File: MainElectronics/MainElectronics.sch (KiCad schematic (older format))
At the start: 11 parts

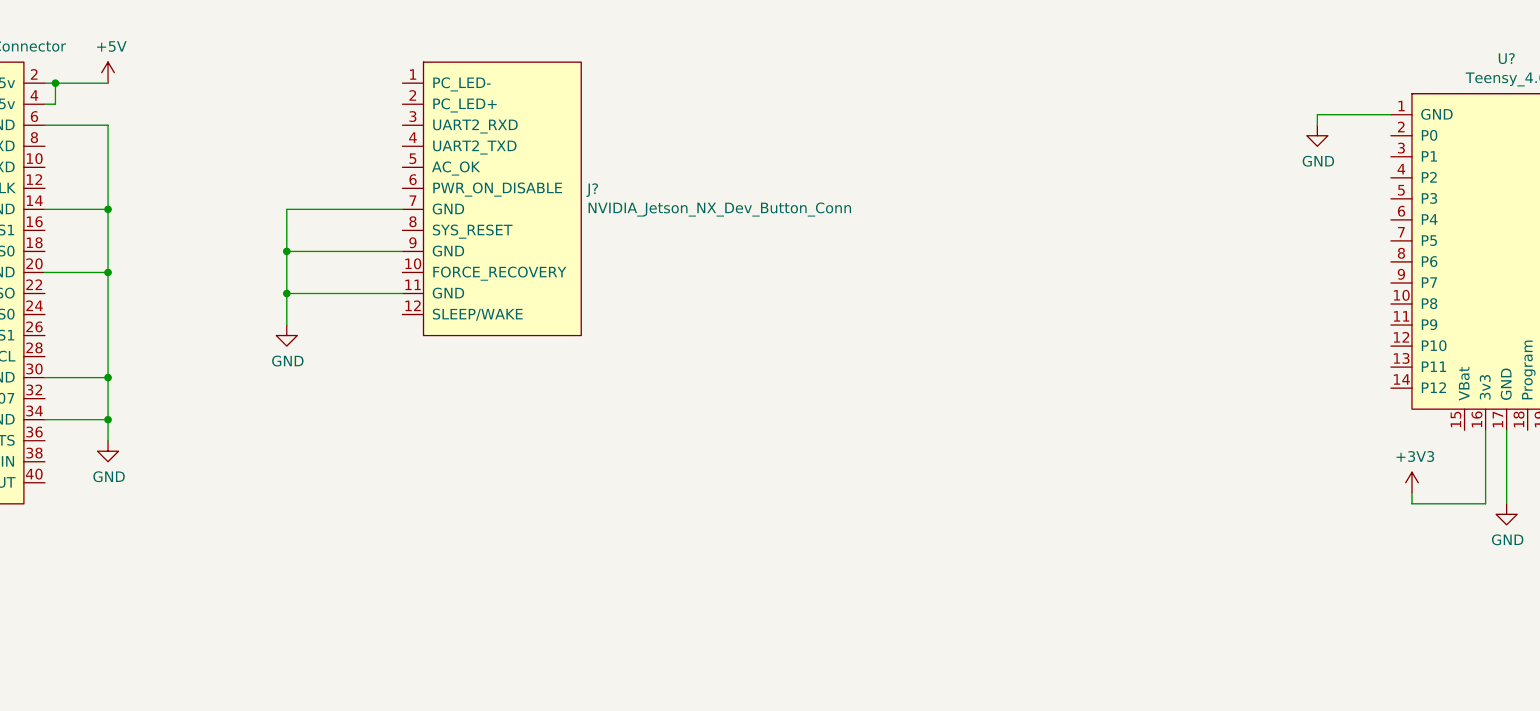
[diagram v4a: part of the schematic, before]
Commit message: Connected Jetson and Teensy
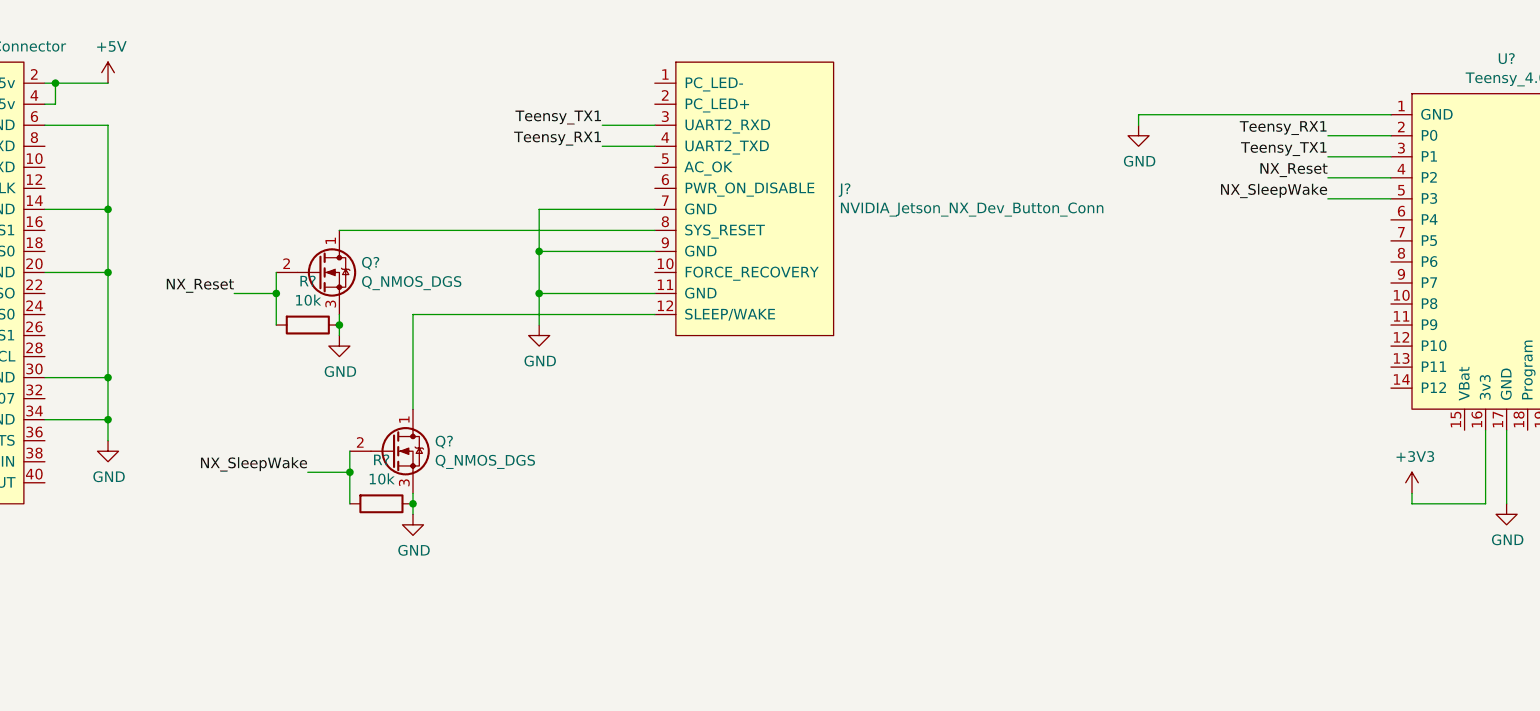
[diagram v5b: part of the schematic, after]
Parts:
- added Q? (x2): Q_NMOS_DGS, symbol Device:Q_NMOS_DGS
- added R? (x2): 10k, symbol Device:R
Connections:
- net GND: now also Q?.3 (S), Q?.3 (S), R?.1, R?.1
- net at J?.12 (SLEEP/WAKE): now also Q?.1 (D)
- net Teensy_TX1: now reaches J?.3 (UART2_RXD)
- net Teensy_TX1: now also U?.3 (P1)
- net Teensy_RX1: now reaches J?.4 (UART2_TXD)
- net Teensy_RX1: now also U?.2 (P0)
- net at J?.8 (SYS_RESET): now also Q?.1 (D)
- net NX_Reset: now reaches U?.4 (P2)
- net NX_Reset: now also Q?.2 (G), R?.2
- net NX_SleepWake: now reaches U?.5 (P3)
- net NX_SleepWake: now also Q?.2 (G), R?.2
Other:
- moved on the sheet: J?
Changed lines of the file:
@@
 L MainElectronicsLib:NVIDIA_Jetson_NX_Dev_Button_Conn J?
 U 1 1 5ED74642
-P 5500 2750
-F 0 "J?" H 5928 3046 50  0000 L CNN
-F 1 "NVIDIA_Jetson_NX_Dev_Button_Conn" H 5928 2955 50  0000 L CNN
-F 2 "" H 5500 3700 50  0001 C CNN
-F 3 "" H 5500 3700 50  0001 C CNN
-	1    5500 2750
+P 6700 2750
+F 0 "J?" H 7128 3046 50  0000 L CNN
+F 1 "NVIDIA_Jetson_NX_Dev_Button_Conn" H 7128 2955 50  0000 L CNN
+F 2 "" H 6700 3700 50  0001 C CNN
+F 3 "" H 6700 3700 50  0001 C CNN
+	1    6700 2750
 	1    0    0    -1
 $EndComp
@@
 L power:GND #PWR?
 U 1 1 5EDF91C0
-P 4500 3100
-F 0 "#PWR?" H 4500 2850 50  0001 C CNN
-F 1 "GND" H 4505 2927 50  0000 C CNN
-F 2 "" H 4500 3100 50  0001 C CNN
-F 3 "" H 4500 3100 50  0001 C CNN
-	1    4500 3100
-	1    0    0    -1
-$EndComp
-Wire Wire Line
-	5050 2550 4500 2550
-Wire Wire Line
-	4500 2550 4500 2750
-Wire Wire Line
-	5050 2750 4500 2750
-Connection ~ 4500 2750
-Wire Wire Line
-	4500 2750 4500 2950
-Wire Wire Line
-	5050 2950 4500 2950
-Connection ~ 4500 2950
-Wire Wire Line
-	4500 2950 4500 3100
+P 5700 3100
+F 0 "#PWR?" H 5700 2850 50  0001 C CNN
+F 1 "GND" H 5705 2927 50  0000 C CNN
+F 2 "" H 5700 3100 50  0001 C CNN
+F 3 "" H 5700 3100 50  0001 C CNN
+	1    5700 3100
+	1    0    0    -1
+$EndComp
+Wire Wire Line
+	6250 2550 5700 2550
+Wire Wire Line
+	5700 2550 5700 2750
+Wire Wire Line
+	6250 2750 5700 2750
+Connection ~ 5700 2750
+Wire Wire Line
+	5700 2750 5700 2950
+Wire Wire Line
+	6250 2950 5700 2950
+Connection ~ 5700 2950
+Wire Wire Line
+	5700 2950 5700 3100
 $Comp
 L power:GND #PWR?
 U 1 1 5EDFB035
-P 9400 2150
-F 0 "#PWR?" H 9400 1900 50  0001 C CNN
-F 1 "GND" H 9405 1977 50  0000 C CNN
-F 2 "" H 9400 2150 50  0001 C CNN
-F 3 "" H 9400 2150 50  0001 C CNN
-	1    9400 2150
-	1    0    0    -1
-$EndComp
-Wire Wire Line
-	9750 2100 9400 2100
-Wire Wire Line
-	9400 2100 9400 2150
+P 8550 2150
+F 0 "#PWR?" H 8550 1900 50  0001 C CNN
+F 1 "GND" H 8555 1977 50  0000 C CNN
+F 2 "" H 8550 2150 50  0001 C CNN
+F 3 "" H 8550 2150 50  0001 C CNN
+	1    8550 2150
+	1    0    0    -1
+$EndComp
+Wire Wire Line
+	9750 2100 8550 2100
+Wire Wire Line
+	8550 2100 8550 2150
 $Comp
 L power:GND #PWR?
@@
 Text Label 11050 3000 0    50   ~ 0
 NEOPIXEL_DIN
+Wire Wire Line
+	9750 2200 9450 2200
+Wire Wire Line
+	9750 2300 9450 2300
+Text Label 9450 2200 2    50   ~ 0
+Teensy_RX1
+Text Label 9450 2300 2    50   ~ 0
+Teensy_TX1
+Text Label 6000 2250 2    50   ~ 0
+Teensy_RX1
+Text Label 6000 2150 2    50   ~ 0
+Teensy_TX1
+Wire Wire Line
+	6000 2150 6250 2150
+Wire Wire Line
+	6250 2250 6000 2250
+Wire Wire Line
+	6250 2650 4750 2650
+Wire Wire Line
+	5100 3500 5100 3050
+Wire Wire Line
+	5100 3050 6250 3050
+$Comp
+L power:GND #PWR?
+U 1 1 5EE9D355
+P 5100 4000
+F 0 "#PWR?" H 5100 3750 50  0001 C CNN
+F 1 "GND" H 5105 3827 50  0000 C CNN
+F 2 "" H 5100 4000 50  0001 C CNN
+F 3 "" H 5100 4000 50  0001 C CNN
+	1    5100 4000
+	1    0    0    -1
+$EndComp
+Wire Wire Line
+	5100 4000 5100 3950
+$Comp
+L Device:R R?
+U 1 1 5EEA2232
+P 4950 3950
+F 0 "R?" V 4743 3950 50  0000 C CNN
+F 1 "10k" V 4834 3950 50  0000 C CNN
+F 2 "" V 4880 3950 50  0001 C CNN
+F 3 "~" H 4950 3950 50  0001 C CNN
+	1    4950 3950
+	0    1    1    0
+$EndComp
+Connection ~ 5100 3950
+Wire Wire Line
+	5100 3950 5100 3900
+Wire Wire Line
+	4800 3950 4800 3800
+Wire Wire Line
+	4800 3800 4600 3800
+Connection ~ 4800 3800
+Wire Wire Line
+	4800 3800 4800 3700
+Text Label 4600 3800 2    50   ~ 0
+NX_SleepWake
+Text Label 4250 2950 2    50   ~ 0
+NX_Reset
+Wire Wire Line
+	4450 2950 4450 3100
+Connection ~ 4450 2950
+Wire Wire Line
+	4450 2950 4250 2950
+Wire Wire Line
+	4450 2850 4450 2950
+Wire Wire Line
+	4750 3100 4750 3050
+Connection ~ 4750 3100
+$Comp
+L Device:R R?
+U 1 1 5EEA357F
+P 4600 3100
+F 0 "R?" V 4393 3100 50  0000 C CNN
+F 1 "10k" V 4484 3100 50  0000 C CNN
+F 2 "" V 4530 3100 50  0001 C CNN
+F 3 "~" H 4600 3100 50  0001 C CNN
+	1    4600 3100
+	0    1    1    0
+$EndComp
+Wire Wire Line
+	4750 3150 4750 3100
+$Comp
+L power:GND #PWR?
+U 1 1 5EE9D73F
+P 4750 3150
+F 0 "#PWR?" H 4750 2900 50  0001 C CNN
+F 1 "GND" H 4755 2977 50  0000 C CNN
+F 2 "" H 4750 3150 50  0001 C CNN
+F 3 "" H 4750 3150 50  0001 C CNN
+	1    4750 3150
+	1    0    0    -1
+$EndComp
+$Comp
+L Device:Q_NMOS_DGS Q?
+U 1 1 5EE9639C
+P 5000 3700
+F 0 "Q?" H 5204 3746 50  0000 L CNN
+F 1 "Q_NMOS_DGS" H 5204 3655 50  0000 L CNN
+F 2 "" H 5200 3800 50  0001 C CNN
+F 3 "~" H 5000 3700 50  0001 C CNN
+	1    5000 3700
+	1    0    0    -1
+$EndComp
+$Comp
+L Device:Q_NMOS_DGS Q?
+U 1 1 5EE91588
+P 4650 2850
+F 0 "Q?" H 4854 2896 50  0000 L CNN
+F 1 "Q_NMOS_DGS" H 4854 2805 50  0000 L CNN
+F 2 "" H 4850 2950 50  0001 C CNN
+F 3 "~" H 4650 2850 50  0001 C CNN
+	1    4650 2850
+	1    0    0    -1
+$EndComp
+Text Label 9450 2400 2    50   ~ 0
+NX_Reset
+Text Label 9450 2500 2    50   ~ 0
+NX_SleepWake
+Wire Wire Line
+	9450 2400 9750 2400
+Wire Wire Line
+	9450 2500 9750 2500
 $EndSCHEMATC

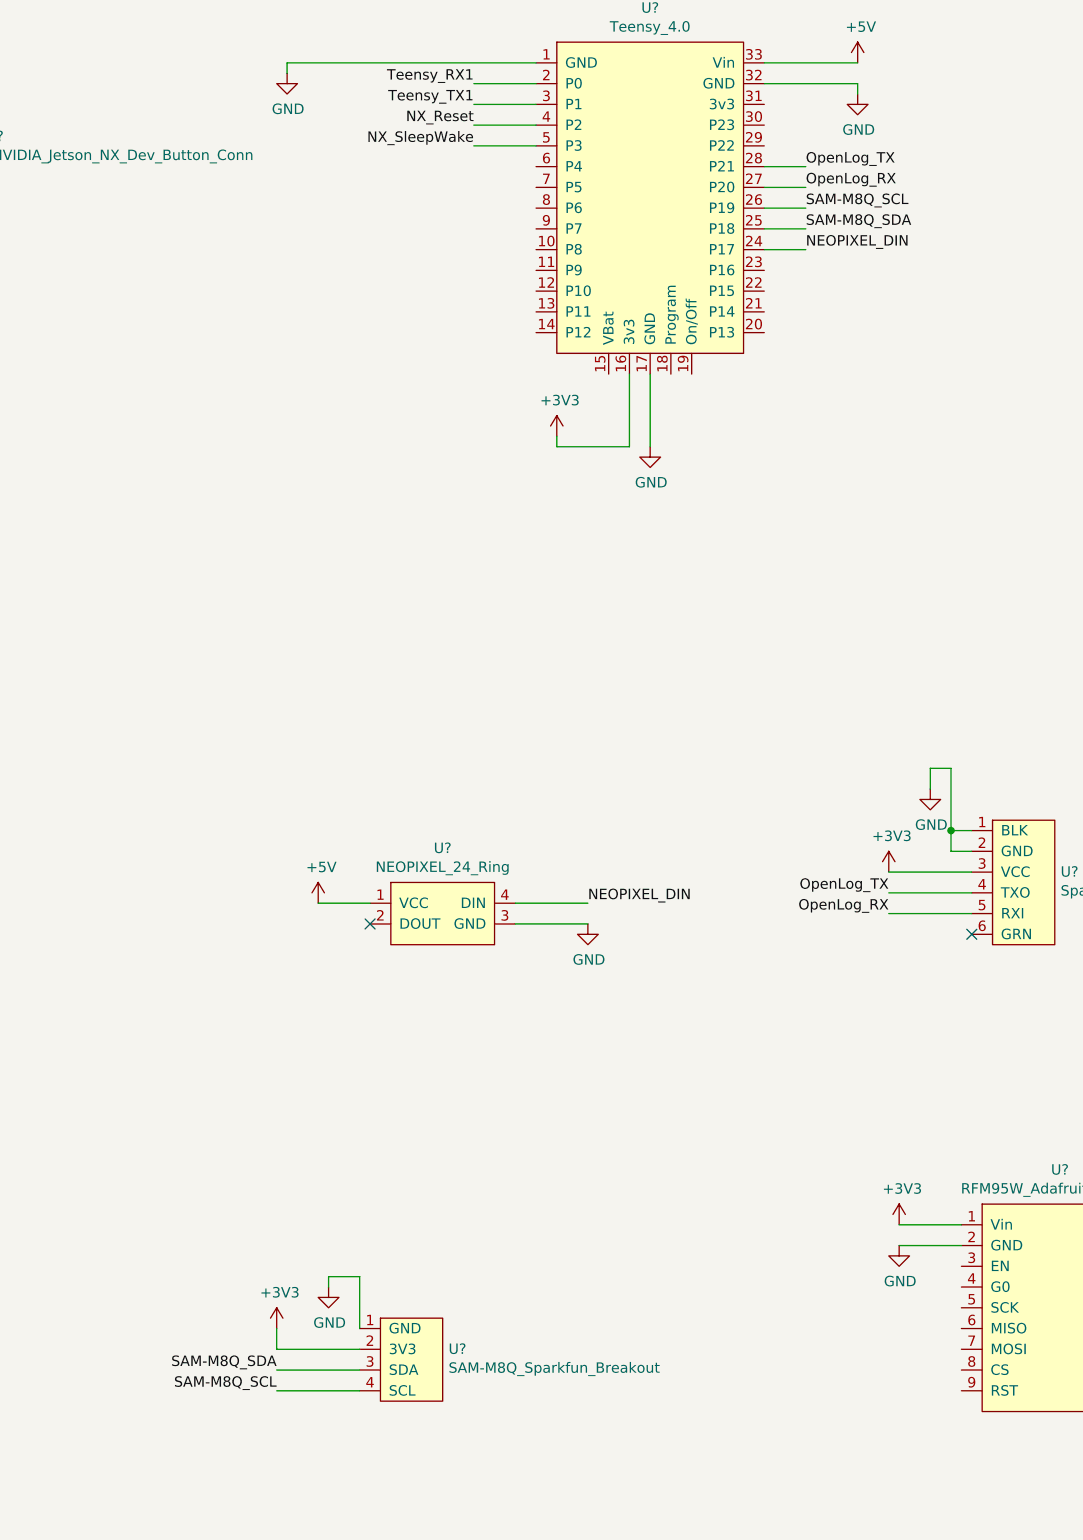
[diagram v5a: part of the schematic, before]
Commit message: Updated some net names to be more consistent
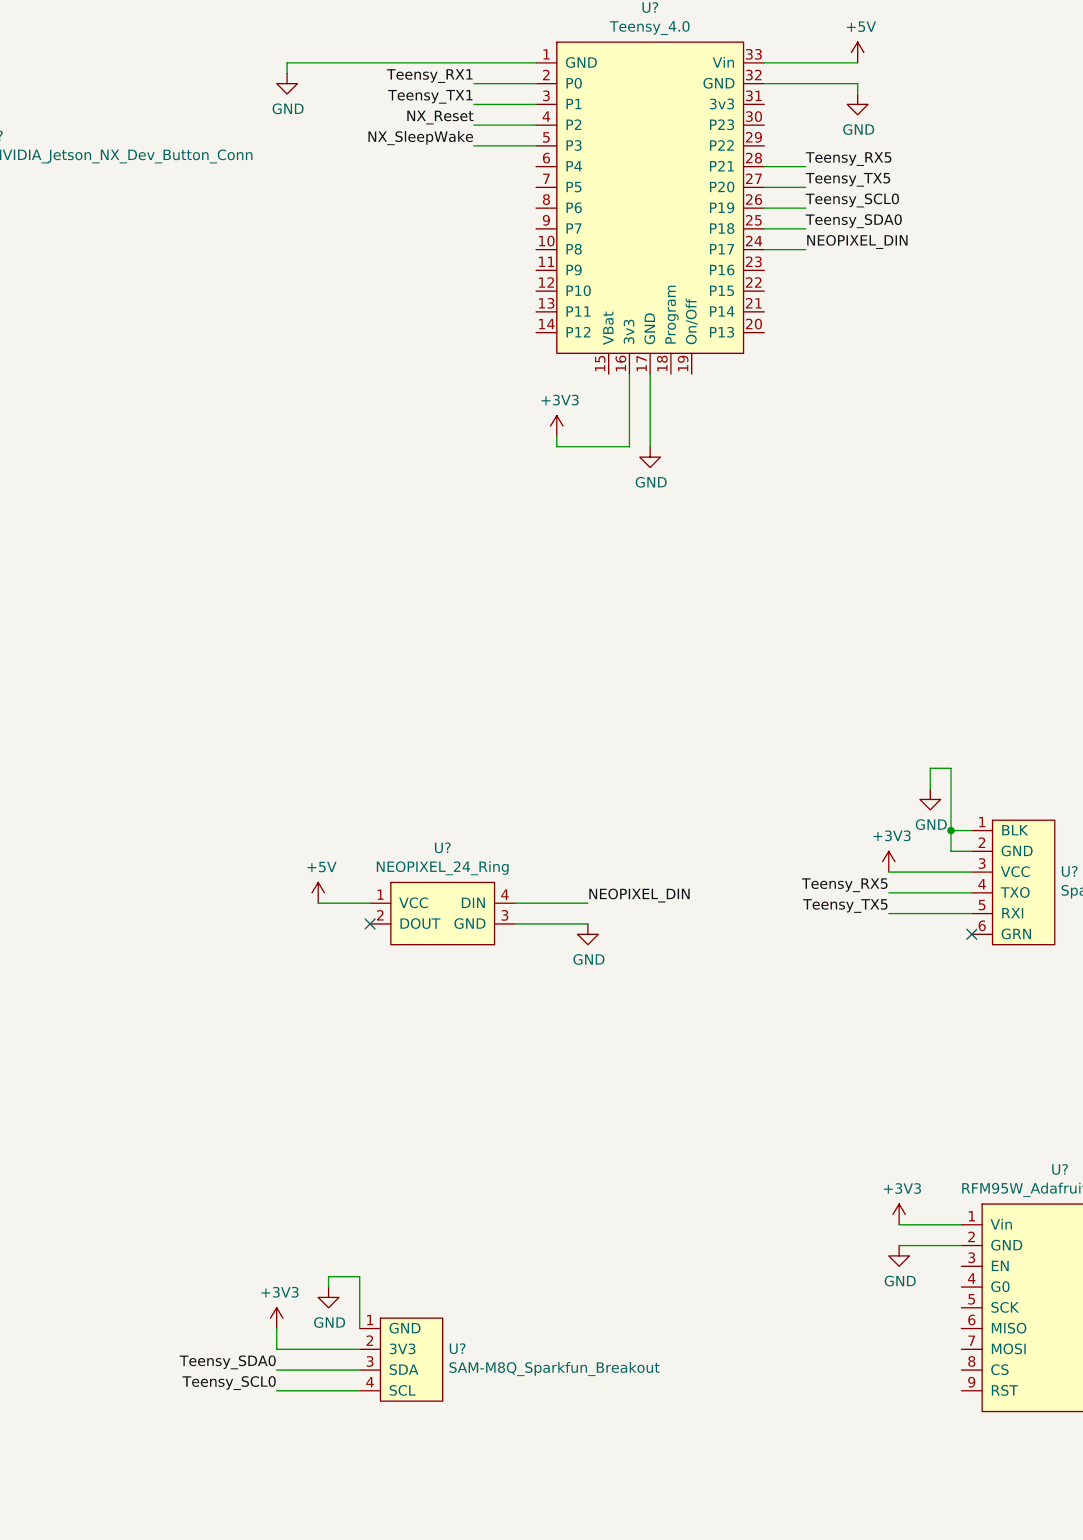
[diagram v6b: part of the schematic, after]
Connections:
- net OpenLog_RX renamed Teensy_TX5
- net OpenLog_TX renamed Teensy_RX5
- net SAM-M8Q_SCL renamed Teensy_SCL0
- net SAM-M8Q_SDA renamed Teensy_SDA0
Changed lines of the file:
@@
 	11850 6200 11450 6200
 Text Label 11450 6100 2    50   ~ 0
-OpenLog_TX
+Teensy_RX5
 Text Label 11450 6200 2    50   ~ 0
-OpenLog_RX
+Teensy_TX5
 Text Label 11050 2600 0    50   ~ 0
-OpenLog_TX
+Teensy_RX5
 Wire Wire Line
 	11050 2600 10850 2600
@@
 	10850 2700 11050 2700
 Text Label 11050 2700 0    50   ~ 0
-OpenLog_RX
+Teensy_TX5
 Wire Wire Line
 	8900 8400 8500 8400
 Wire Wire Line
 	8900 8500 8500 8500
-Text Label 8500 8400 2    50   ~ 0
-SAM-M8Q_SDA
-Text Label 8500 8500 2    50   ~ 0
-SAM-M8Q_SCL
 Text Label 11050 2900 0    50   ~ 0
-SAM-M8Q_SDA
+Teensy_SDA0
 Text Label 11050 2800 0    50   ~ 0
-SAM-M8Q_SCL
+Teensy_SCL0
 Wire Wire Line
 	11050 2800 10850 2800
@@
 Wire Wire Line
 	9450 2500 9750 2500
+Text Label 8500 8500 2    50   ~ 0
+Teensy_SCL0
+Text Label 8500 8400 2    50   ~ 0
+Teensy_SDA0
 $EndSCHEMATC
